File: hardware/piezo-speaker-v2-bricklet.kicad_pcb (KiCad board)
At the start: 2 copper layers, 45 x 55 mm, 41 parts, among them P1 CON-SENSOR2, P2 BOOT, P3 DEBUG, P4 PT-4532PLQ, Q101 2N7002P, U1 XMC1XXX24, U2 LD1117, U3 LMR62014X, U4 DRILL, U5 DRILL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

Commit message: drc
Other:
- rule pad_to_mask_clearance: 0.2 -> 0
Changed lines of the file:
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@@
     (pad_size 1.524 1.524)
     (pad_drill 0.762)
-    (pad_to_mask_clearance 0.2)
-    (solder_mask_min_width 0.25)
+    (pad_to_mask_clearance 0)
     (aux_axis_origin 0 0)
     (visible_elements FFFEFF7F)
@@
       (psnegative false)
       (psa4output false)
-      (plotreference true)
-      (plotvalue true)
+      (plotreference false)
+      (plotvalue false)
       (plotinvisibletext false)
       (padsonsilk false)

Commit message: specify rp3 to 33k
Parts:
- RP3: value 34k -> 33k
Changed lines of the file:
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@@
   (layers
     (0 F.Cu signal)
-    (31 B.Cu signal)
+    (31 B.Cu signal hide)
     (32 B.Adhes user)
     (33 F.Adhes user)
@@
     (pad_drill 0.762)
     (pad_to_mask_clearance 0)
+    (solder_mask_min_width 0.25)
     (aux_axis_origin 0 0)
     (visible_elements FFFEFF7F)
@@
       (effects (font (size 0.29972 0.29972) (thickness 0.07493)))
     )
-    (fp_text value 34k (at 1.01 -0.02) (layer F.Fab)
+    (fp_text value 33k (at 1.01 -0.02) (layer F.Fab)
       (effects (font (size 0.29972 0.29972) (thickness 0.07493)))
     )

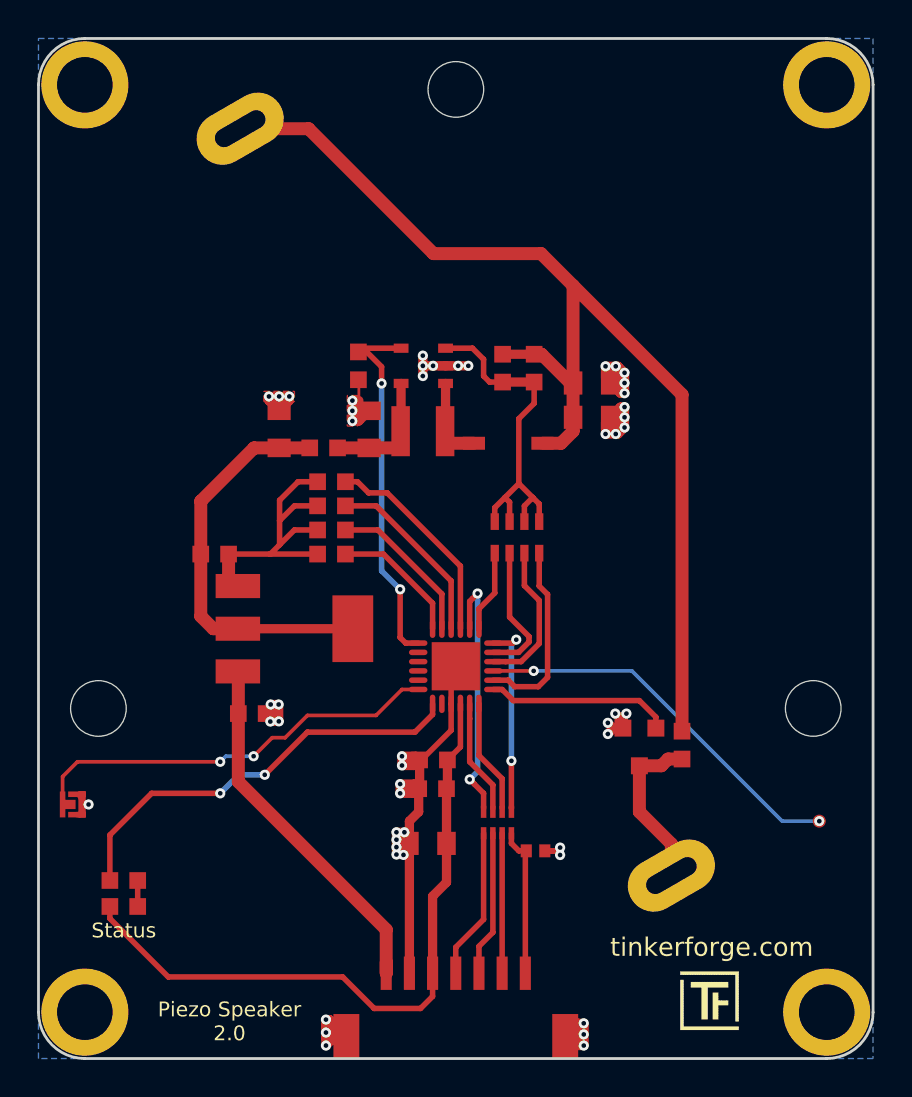
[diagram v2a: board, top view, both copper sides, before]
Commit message: add fiducial marks
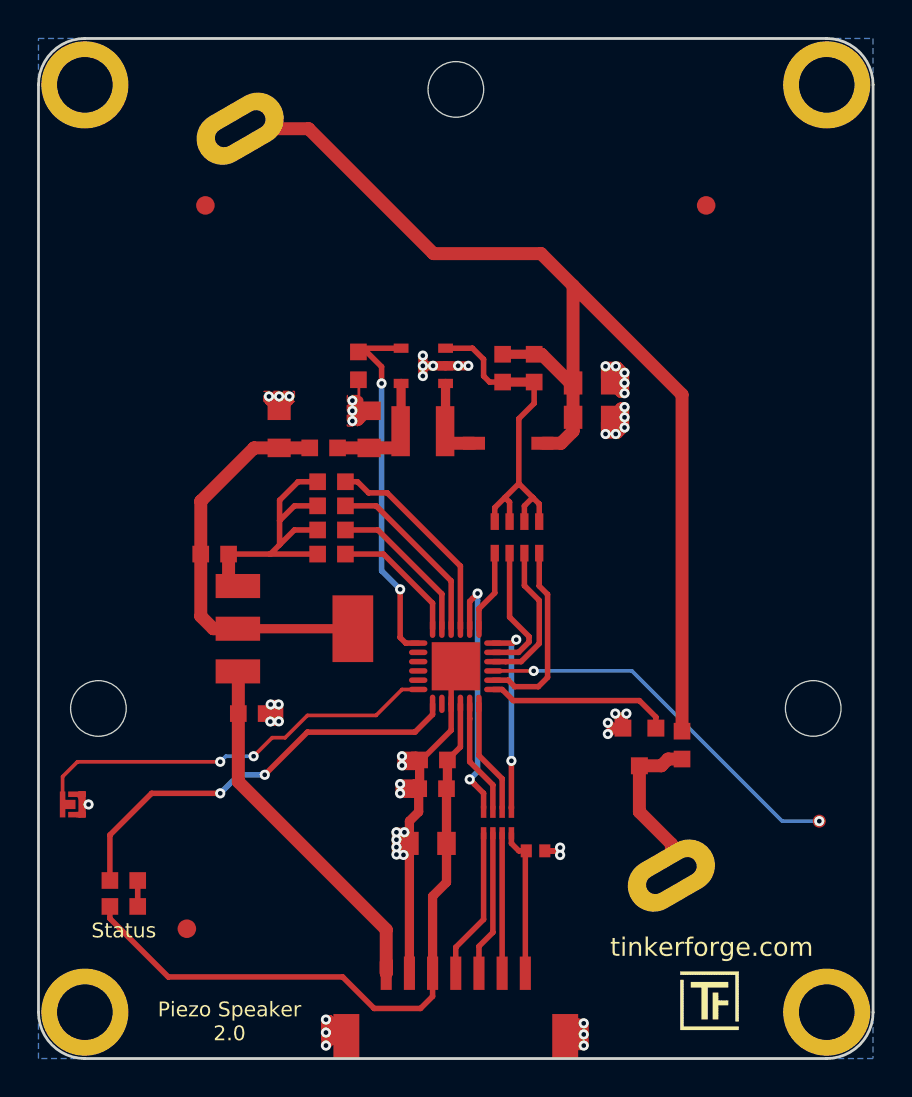
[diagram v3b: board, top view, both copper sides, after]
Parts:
- added Fiducial_Mark: VAL**, kicad-libraries:Fiducial_Mark, F.Cu at (140.5, 123.0)
- added Fiducial_Mark: VAL**, kicad-libraries:Fiducial_Mark, F.Cu at (168.5, 84.0)
- added Fiducial_Mark: VAL**, kicad-libraries:Fiducial_Mark, F.Cu at (141.5, 84.0)
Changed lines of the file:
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@@
     (tracks 438)
     (zones 0)
-    (modules 41)
+    (modules 44)
     (nets 33)
   )
@@
     (pad_to_mask_clearance 0)
     (solder_mask_min_width 0.25)
-    (aux_axis_origin 0 0)
+    (aux_axis_origin 132.5 130)
+    (grid_origin 132.5 130)
     (visible_elements FFFEFF7F)
     (pcbplotparams
@@
     )
   )
+  (module kicad-libraries:Fiducial_Mark (layer F.Cu)
+    (at 140.5 123)
+    (attr smd)
+    (fp_text reference Fiducial_Mark (at 0 0) (layer F.SilkS) hide
+      (effects (font (size 0.127 0.127) (thickness 0.03302)))
+    )
+    (fp_text value VAL** (at 0 -0.29972) (layer F.SilkS) hide
+      (effects (font (size 0.127 0.127) (thickness 0.03302)))
+    )
+    (fp_circle (center 0 0) (end 1.15062 0) (layer Dwgs.User) (width 0.01016))
+    (pad 1 smd circle (at 0 0) (size 1.00076 1.00076) (layers F.Cu F.Paste F.Mask)
+      (clearance 0.65024))
+  )
+  (module kicad-libraries:Fiducial_Mark (layer F.Cu)
+    (at 168.5 84)
+    (attr smd)
+    (fp_text reference Fiducial_Mark (at 0 0) (layer F.SilkS) hide
+      (effects (font (size 0.127 0.127) (thickness 0.03302)))
+    )
+    (fp_text value VAL** (at 0 -0.29972) (layer F.SilkS) hide
+      (effects (font (size 0.127 0.127) (thickness 0.03302)))
+    )
+    (fp_circle (center 0 0) (end 1.15062 0) (layer Dwgs.User) (width 0.01016))
+    (pad 1 smd circle (at 0 0) (size 1.00076 1.00076) (layers F.Cu F.Paste F.Mask)
+      (clearance 0.65024))
+  )
+  (module kicad-libraries:Fiducial_Mark (layer F.Cu)
+    (at 141.5 84)
+    (attr smd)
+    (fp_text reference Fiducial_Mark (at 0 0) (layer F.SilkS) hide
+      (effects (font (size 0.127 0.127) (thickness 0.03302)))
+    )
+    (fp_text value VAL** (at 0 -0.29972) (layer F.SilkS) hide
+      (effects (font (size 0.127 0.127) (thickness 0.03302)))
+    )
+    (fp_circle (center 0 0) (end 1.15062 0) (layer Dwgs.User) (width 0.01016))
+    (pad 1 smd circle (at 0 0) (size 1.00076 1.00076) (layers F.Cu F.Paste F.Mask)
+      (clearance 0.65024))
+  )
   (gr_line (start 132.5 77.5) (end 132.5 127.5) (angle 90) (layer Edge.Cuts) (width 0.15))

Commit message: changed processor to XMC1100
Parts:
- U1: value XMC1XXX24 -> XMC1100
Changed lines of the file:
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@@
       (effects (font (size 0.3 0.3) (thickness 0.075)))
     )
-    (fp_text value XMC1XXX24 (at 0 0.8) (layer F.Fab)
+    (fp_text value XMC1100 (at 0 0.8) (layer F.Fab)
       (effects (font (size 0.3 0.3) (thickness 0.075)))
     )

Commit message: specify ld1117-adj
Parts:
- U2: value LD1117 -> LD1117-ADJ
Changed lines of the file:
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@@
       (effects (font (size 0.29972 0.29972) (thickness 0.07493)))
     )
-    (fp_text value LD1117 (at 0 0 270) (layer F.Fab)
+    (fp_text value LD1117-ADJ (at 0 0 270) (layer F.Fab)
       (effects (font (size 0.29972 0.29972) (thickness 0.07493)))
     )
